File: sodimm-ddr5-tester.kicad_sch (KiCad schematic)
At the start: 14 parts, among them M1001 Mech_Lightpipe_Mentor_1296.20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

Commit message: Sync new components with PCB
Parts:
- gave numbers to parts that had none: 1

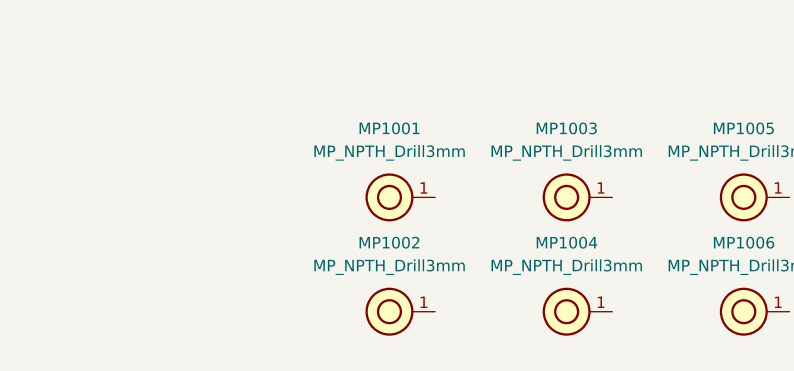
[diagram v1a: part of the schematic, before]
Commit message: Fix PCIE directions, place and route RFU/detect DDR signal components
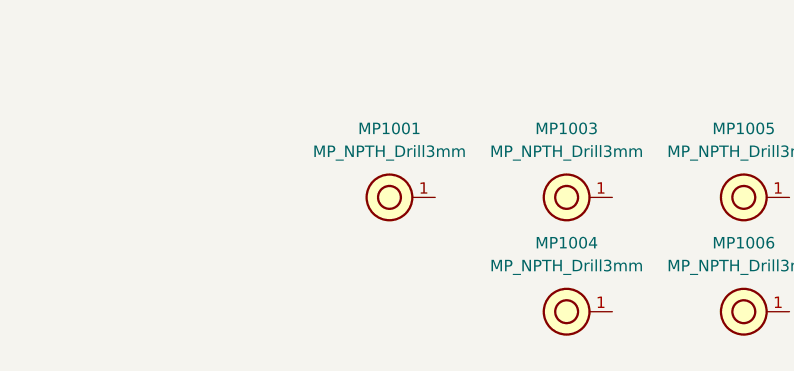
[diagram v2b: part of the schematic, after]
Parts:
- removed MP1002: MP_NPTH_Drill3mm, sodimm-ddr5-tester-footprints:MP_NPTH_Drill3mm, symbol sodimm-ddr5-tester:MP_NPTH_Drill3mm
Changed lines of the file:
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@@
-    (pin "1")
-  )
-  (symbol (lib_id "sodimm-ddr5-tester:MP_NPTH_Drill3mm") (at 118.11 278.13 180) (unit 1)
-    (in_bom yes) (on_board yes) (fields_autoplaced)
-    (property "Reference" "MP1002" (id 0) (at 113.03 270.51 0)
-      (effects (font (size 1.27 1.27) (thickness 0.15)))
-    )
-    (property "Value" "MP_NPTH_Drill3mm" (id 1) (at 113.03 273.05 0)
-      (effects (font (size 1.27 1.27) (thickness 0.15)))
-    )
-    (property "Footprint" "sodimm-ddr5-tester-footprints:MP_NPTH_Drill3mm" (id 2) (at 100.33 270.51 0)
-      (effects (font (size 1.27 1.27) (thickness 0.15)) (justify left bottom) hide)
-    )
-    (property "Datasheet" "" (id 3) (at 101.27 262.56 0)
-      (effects (font (size 1.27 1.27) (thickness 0.15)) (justify left bottom) hide)
-    )
-    (property "Author" "Antmicro" (id 4) (at 100.33 267.97 0)
-      (effects (font (size 1.27 1.27) (thickness 0.15)) (justify left bottom) hide)
-    )
-    (property "License" "Apache-2.0" (id 5) (at 100.33 265.43 0)
-      (effects (font (size 1.27 1.27) (thickness 0.15)) (justify left bottom) hide)
-    )
     (pin "1")
   )
@@
       (reference "#PWR04001") (unit 1) (value "GND") (footprint "")
     )
-    (path "/00000000-0000-0000-0000-000061827943/b4fe4b21-605e-47bb-8b05-0e869addbac3"
-      (reference "#PWR04002") (unit 1) (value "GND") (footprint "")
-    )
-    (path "/00000000-0000-0000-0000-000061827943/24fe28f1-a309-4ec0-8a23-620efefad4d7"
-      (reference "#PWR04003") (unit 1) (value "GND") (footprint "")
-    )
-    (path "/00000000-0000-0000-0000-000061827943/d8fd3129-5a7e-4686-938d-78acda3c6d8d"
-      (reference "#PWR04004") (unit 1) (value "GND") (footprint "")
-    )
     (path "/00000000-0000-0000-0000-0000600295c1/e82edc94-9cb6-4bf4-a822-76d1bcf5d967"
       (reference "#PWR05002") (unit 1) (value "GND") (footprint "")
@@
       (reference "#PWR05115") (unit 1) (value "GND") (footprint "")
     )
-    (path "/00000000-0000-0000-0000-0000600295c1/47c3cd30-e125-4d97-bbad-7a0cf10854d3"
-      (reference "#PWR05116") (unit 1) (value "GND") (footprint "")
-    )
     (path "/00000000-0000-0000-0000-0000600295c1/c5a89fa4-84d8-4d0f-8b2a-9faf2a772151"
       (reference "#PWR05117") (unit 1) (value "GND") (footprint "")
@@
       (reference "#PWR012001") (unit 1) (value "GND") (footprint "")
     )
-    (path "/fea793c3-bc28-42ef-95e7-45c2f3eee090/c715319b-c2a0-403e-8962-431afb761506"
-      (reference "#PWR012002") (unit 1) (value "GND") (footprint "")
-    )
-    (path "/fea793c3-bc28-42ef-95e7-45c2f3eee090/11801b77-fa5f-4cf9-bca3-d81b0fd01bfd"
-      (reference "#PWR012003") (unit 1) (value "GND") (footprint "")
-    )
     (path "/fea793c3-bc28-42ef-95e7-45c2f3eee090/12aa1715-23f0-4d9b-9e7f-a652d10313c8"
       (reference "#PWR012005") (unit 1) (value "GND") (footprint "")
     )
+    (path "/fea793c3-bc28-42ef-95e7-45c2f3eee090/8b872bed-7da7-44df-bbf6-f7d9f37ee9fe"
+      (reference "#PWR?") (unit 1) (value "GND") (footprint "")
+    )
     (path "/00000000-0000-0000-0000-000060225b0c/00000000-0000-0000-0000-000062929c36"
       (reference "1V0") (unit 1) (value "TP_1mm_SMD") (footprint "sodimm-ddr5-tester-footprints:Testpoint_smd_1mm")
@@
       (reference "C5065") (unit 1) (value "C_100n_0402") (footprint "sodimm-ddr5-tester-footprints:C_0402_1005Metric_EIA")
     )
-    (path "/00000000-0000-0000-0000-0000600295c1/74cca571-e806-4a6c-9d93-153be2a79667"
-      (reference "C5066") (unit 1) (value "C_100n_0402") (footprint "sodimm-ddr5-tester-footprints:C_0402_1005Metric_EIA")
-    )
     (path "/00000000-0000-0000-0000-0000600295c1/17d64bc2-4ee9-4ba9-a384-672c0e940bb9"
       (reference "C5067") (unit 1) (value "C_100n_0402") (footprint "sodimm-ddr5-tester-footprints:C_0402_1005Metric_EIA")
@@
       (reference "J3001") (unit 1) (value "PinHeader_2x7_P2mm_SMD_Shrouded_no-locator") (footprint "sodimm-ddr5-tester-footprints:PinHeader_2x7_P2mm_SMD_Shrouded_no-locator")
     )
-    (path "/00000000-0000-0000-0000-000061827943/8b18d11c-d386-4fa0-9e06-e20c417cce48"
-      (reference "J4001") (unit 1) (value "BUS_DDR5_SODIMM_AMPHENOL_10161033-002RHLF") (footprint "sodimm-ddr5-tester-footprints:DDR5_AMPHENOL_10161033-002RHLF")
-    )
-    (path "/00000000-0000-0000-0000-000061827943/766577bd-927f-4578-8221-16a90fdabacf"
-      (reference "J4001") (unit 2) (value "BUS_DDR5_SODIMM_AMPHENOL_10161033-002RHLF") (footprint "sodimm-ddr5-tester-footprints:DDR5_AMPHENOL_10161033-002RHLF")
+    (path "/00000000-0000-0000-0000-000061827943/7a6df880-a1c1-4bf3-a388-5511bb77ca7a"
+      (reference "J4001") (unit 1) (value "BUS_DDR5_SODIMM_AMPHENOL_10161033-002RHLF") (footprint "antmicro-footprints:DDR5_AMPHENOL_10161033-002RHLF")
+    )
+    (path "/00000000-0000-0000-0000-000061827943/5b2ce360-f66c-48d7-9f64-50bfcb840d1c"
+      (reference "J4001") (unit 2) (value "BUS_DDR5_SODIMM_AMPHENOL_10161033-002RHLF") (footprint "antmicro-footprints:DDR5_AMPHENOL_10161033-002RHLF")
     )
     (path "/00000000-0000-0000-0000-0000600e76d8/5131a49b-2ef0-4a17-98fb-5d86ff6d6ac7"
@@
       (reference "J10001") (unit 1) (value "JST_SH_1x4_BM04B-SRSS-TB-LF-SN") (footprint "sodimm-ddr5-tester-footprints:Conn_JST_SH_1x4_BM04B-SRSS-TB-LF-SN")
     )
-    (path "/fea793c3-bc28-42ef-95e7-45c2f3eee090/03677037-7bb6-41ad-a547-02ff23264f1a"
-      (reference "J12001") (unit 1) (value "PCIe_x4_Conn_Edge") (footprint "sodimm-ddr5-tester-footprints:PCIexpress_x4_Card")
+    (path "/fea793c3-bc28-42ef-95e7-45c2f3eee090/32da38f4-116d-42ab-bdaa-ccdc29bb171f"
+      (reference "J12001") (unit 1) (value "Edge_Conn_Bus_PCIe_x4") (footprint "antmicro-footprints:BUS_PCIexpress_x4")
     )
     (path "/00000000-0000-0000-0000-000060225b0c/e3e99055-6fc1-4be4-ae3b-c17db36deb94"
@@
       (reference "MP1001") (unit 1) (value "MP_NPTH_Drill3mm") (footprint "sodimm-ddr5-tester-footprints:MP_NPTH_Drill3mm")
     )
-    (path "/341a4d20-f8d4-49d6-b5c0-2d2ce06cfbe6"
-      (reference "MP1002") (unit 1) (value "MP_NPTH_Drill3mm") (footprint "sodimm-ddr5-tester-footprints:MP_NPTH_Drill3mm")
-    )
     (path "/7d08de2b-dea6-4e18-a92c-d592e2ac193f"

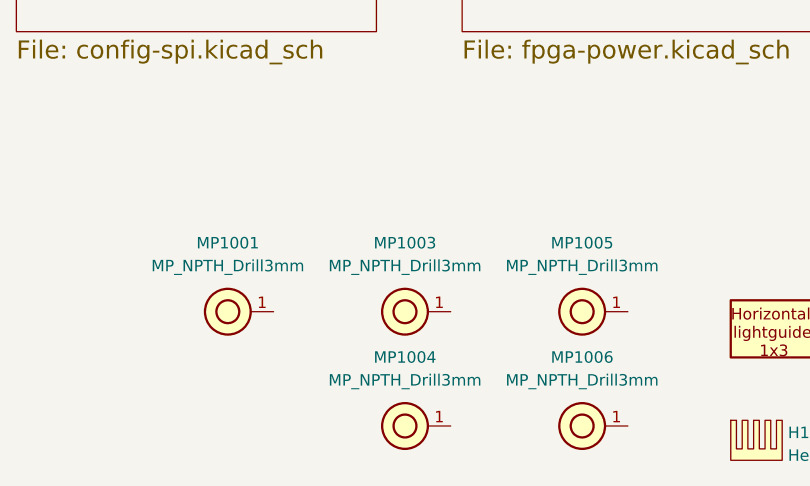
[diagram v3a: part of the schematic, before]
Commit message: Finish routing after schematic modification, optimize power planes
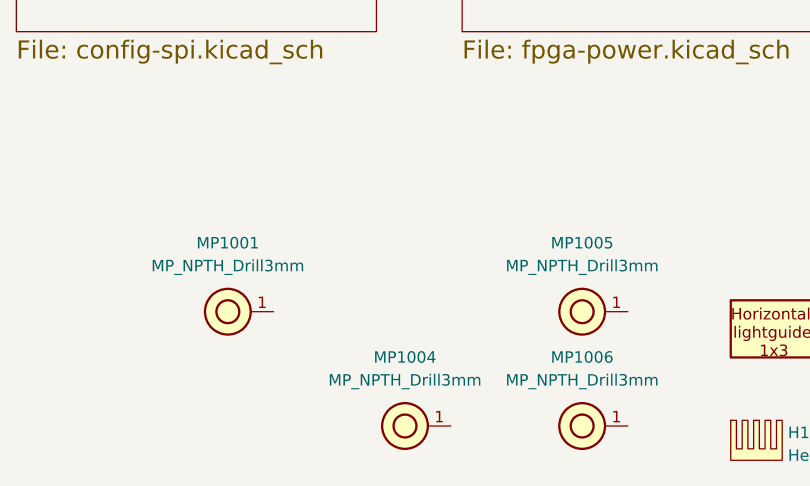
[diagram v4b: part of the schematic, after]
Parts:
- removed MP1003: MP_NPTH_Drill3mm, sodimm-ddr5-tester-footprints:MP_NPTH_Drill3mm, symbol sodimm-ddr5-tester:MP_NPTH_Drill3mm
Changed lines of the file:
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@@
     )
-  )
-  (symbol (lib_id "sodimm-ddr5-tester:MP_NPTH_Drill3mm") (at 137.795 265.43 180) (unit 1)
-    (in_bom yes) (on_board yes) (fields_autoplaced)
-    (property "Reference" "MP1003" (id 0) (at 132.715 257.81 0)
-      (effects (font (size 1.27 1.27) (thickness 0.15)))
-    )
-    (property "Value" "MP_NPTH_Drill3mm" (id 1) (at 132.715 260.35 0)
-      (effects (font (size 1.27 1.27) (thickness 0.15)))
-    )
-    (property "Footprint" "sodimm-ddr5-tester-footprints:MP_NPTH_Drill3mm" (id 2) (at 120.015 257.81 0)
-      (effects (font (size 1.27 1.27) (thickness 0.15)) (justify left bottom) hide)
-    )
-    (property "Datasheet" "" (id 3) (at 120.955 249.86 0)
-      (effects (font (size 1.27 1.27) (thickness 0.15)) (justify left bottom) hide)
-    )
-    (property "Author" "Antmicro" (id 4) (at 120.015 255.27 0)
-      (effects (font (size 1.27 1.27) (thickness 0.15)) (justify left bottom) hide)
-    )
-    (property "License" "Apache-2.0" (id 5) (at 120.015 252.73 0)
-      (effects (font (size 1.27 1.27) (thickness 0.15)) (justify left bottom) hide)
-    )
-    (pin "1")
   )
   (symbol (lib_id "antmicroMechanicalParts:Heatsink_960-27-12-D-AB-0") (at 168.91 277.495 0) (unit 1)
@@
       (reference "#PWR0151") (unit 1) (value "GND") (footprint "")
     )
+    (path "/fea793c3-bc28-42ef-95e7-45c2f3eee090/8b872bed-7da7-44df-bbf6-f7d9f37ee9fe"
+      (reference "#PWR0152") (unit 1) (value "GND") (footprint "")
+    )
     (path "/00000000-0000-0000-0000-0000600e76d8/7aee2d49-aaf1-4b04-b6a0-0298f9017393"
       (reference "#PWR0153") (unit 1) (value "+3V3") (footprint "")
@@
       (reference "#PWR012005") (unit 1) (value "GND") (footprint "")
     )
-    (path "/fea793c3-bc28-42ef-95e7-45c2f3eee090/8b872bed-7da7-44df-bbf6-f7d9f37ee9fe"
-      (reference "#PWR?") (unit 1) (value "GND") (footprint "")
-    )
     (path "/00000000-0000-0000-0000-000060225b0c/00000000-0000-0000-0000-000062929c36"
       (reference "1V0") (unit 1) (value "TP_1mm_SMD") (footprint "sodimm-ddr5-tester-footprints:Testpoint_smd_1mm")
@@
       (reference "MP1001") (unit 1) (value "MP_NPTH_Drill3mm") (footprint "sodimm-ddr5-tester-footprints:MP_NPTH_Drill3mm")
     )
-    (path "/7d08de2b-dea6-4e18-a92c-d592e2ac193f"
-      (reference "MP1003") (unit 1) (value "MP_NPTH_Drill3mm") (footprint "sodimm-ddr5-tester-footprints:MP_NPTH_Drill3mm")
-    )
     (path "/5af43ecc-69a2-4588-8c89-e6c59b84a82f"
       (reference "MP1004") (unit 1) (value "MP_NPTH_Drill3mm") (footprint "sodimm-ddr5-tester-footprints:MP_NPTH_Drill3mm")
@@
       (reference "TP10004") (unit 1) (value "TP_0.75mm_SMD") (footprint "sodimm-ddr5-tester-footprints:TP_SMD_0.75mm")
     )
-    (path "/00000000-0000-0000-0000-000060225b0c/6ff834b1-749f-48be-a208-8b310bcf950a"
-      (reference "TP10005") (unit 1) (value "TP_0.75mm_SMD") (footprint "sodimm-ddr5-tester-footprints:TP_SMD_0.75mm")
-    )
     (path "/00000000-0000-0000-0000-000060225b0c/633f5b04-6889-489b-8184-1c60fe36f737"

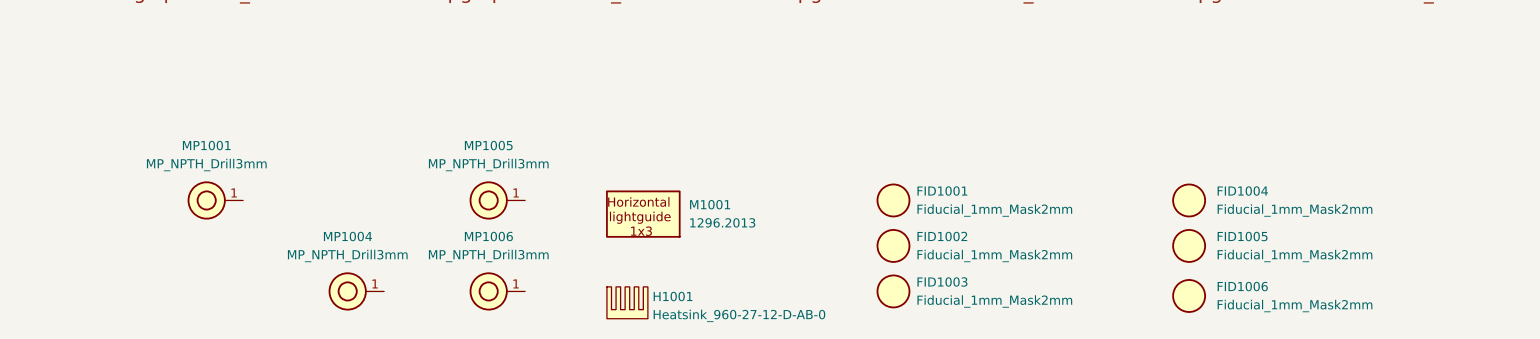
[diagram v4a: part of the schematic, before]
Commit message: Optimize BOM, replace obsolete parts, improve manufacturing attributes
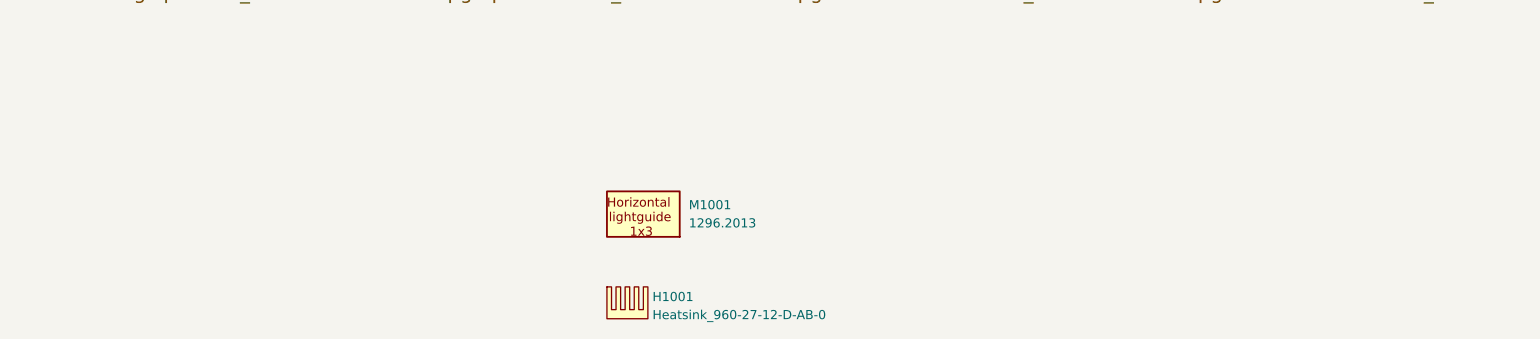
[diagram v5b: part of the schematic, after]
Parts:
- removed FID1001, FID1002, FID1003, FID1004, FID1005, FID1006: Fiducial_1mm_Mask2mm, sodimm-ddr5-tester-footprints:Fiducial_1mm_Mask2mm, symbol sodimm-ddr5-tester:Fiducial_1mm_Mask2mm
- removed MP1001, MP1004, MP1005, MP1006: MP_NPTH_Drill3mm, sodimm-ddr5-tester-footprints:MP_NPTH_Drill3mm, symbol sodimm-ddr5-tester:MP_NPTH_Drill3mm
